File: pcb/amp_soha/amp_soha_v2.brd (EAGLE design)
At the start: 83.9 x 48.9 mm, 59 parts, among them IC1 NE5535U, IC2 7812, IC3 7912, Q1 J113, Q2 J113, Q3 J113, Q4 J113

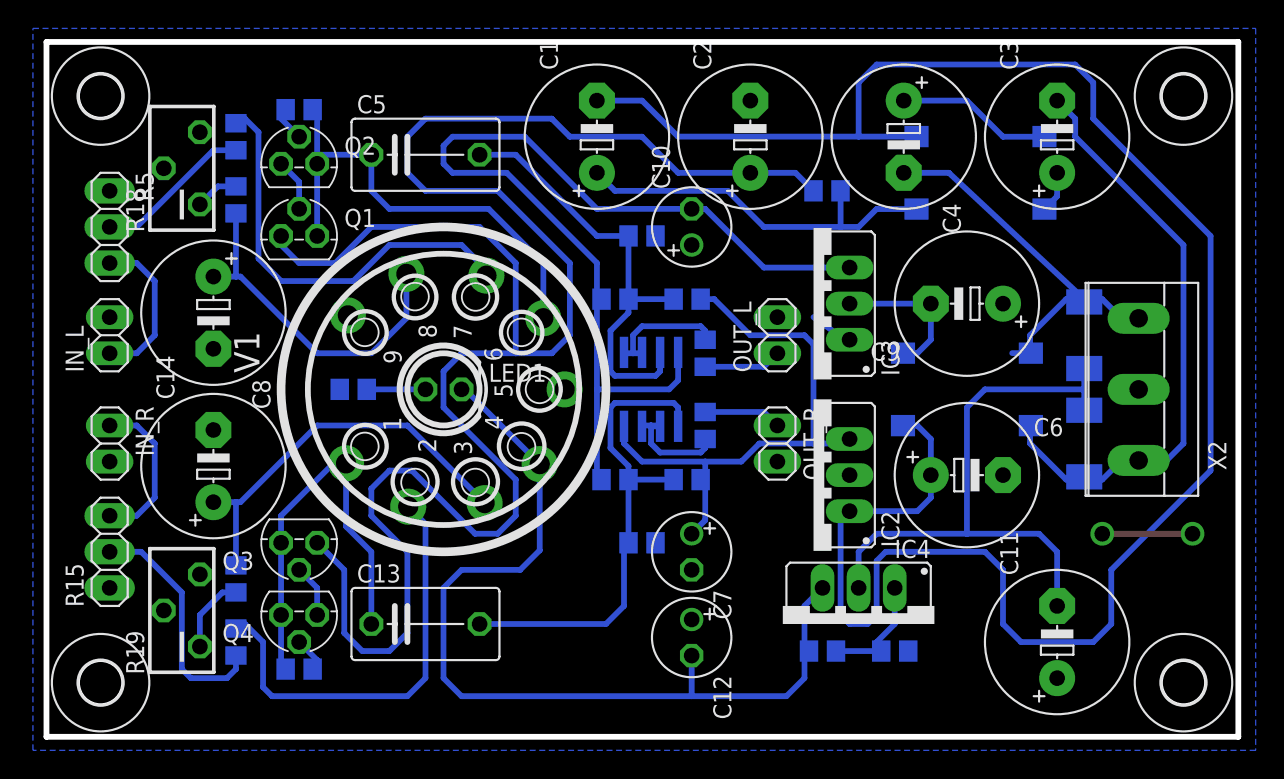
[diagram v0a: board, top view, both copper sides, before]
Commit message: 
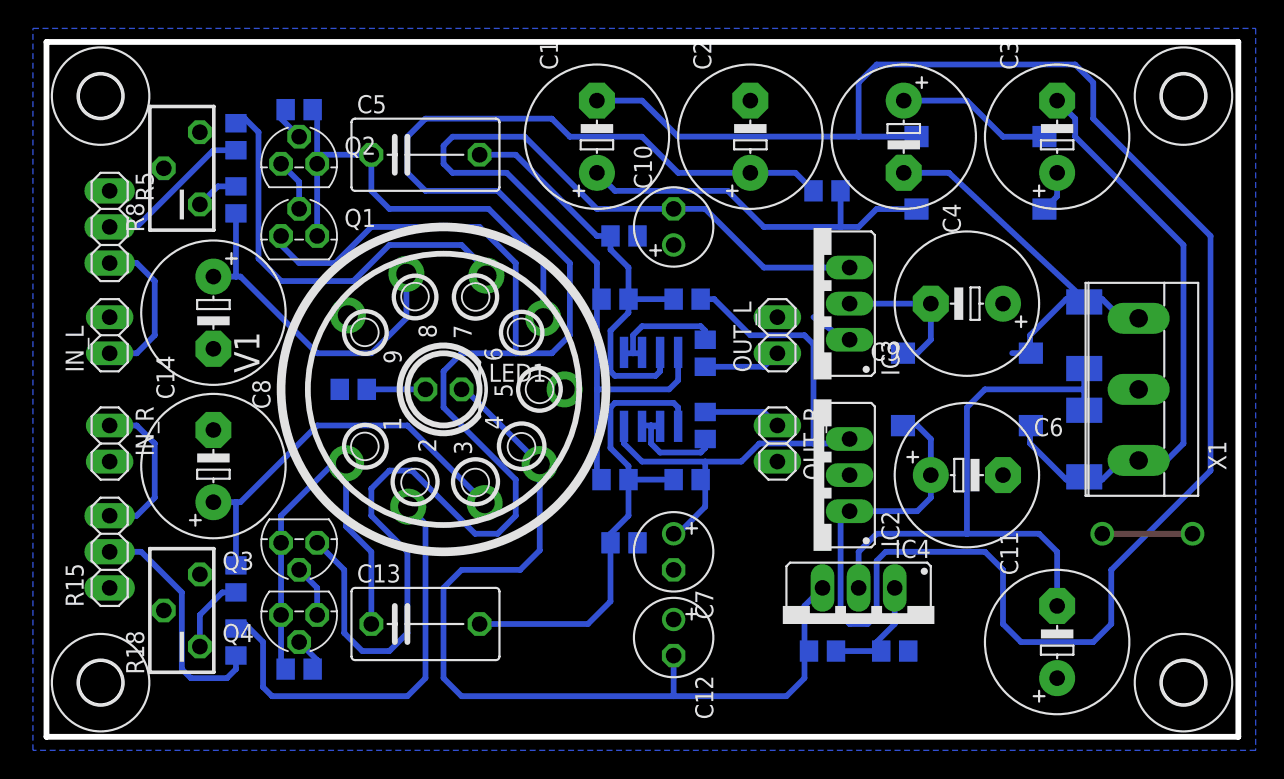
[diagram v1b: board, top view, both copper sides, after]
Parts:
- removed R19: (no value), amp_soha:RTRIM3296Y
- added R8: 2k, amp_soha:RTRIM3296Y
- R10: value (none) -> 1k
- R12, R2: value 360 -> 1k5
- R18: value (none) -> 2k
- moved R18 31.1 mm to (12.1, 9.84)
- moved C10 1.27 mm to (46.7, 36.8)
- moved C12 1.27 mm to (46.7, 7.94)
- moved C7 1.27 mm to (46.7, 14.0)
- moved R14 1.27 mm to (43.2, 14.6)
- moved R4 1.27 mm to (43.2, 36.2)
- renumbered X2 to X1
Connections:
- net AGND: now also R8.2, R8.3; no longer R19.2, R19.3
- net N$17: now also R8.1; no longer R18.1
- net N$18: now also R18.1; no longer R19.1
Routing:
- net N$34: track 35.9 -> 34.4 mm
- net N$22: track 33.1 -> 32.0 mm
- net +12V: track 41.5 -> 42.2 mm

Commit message: 
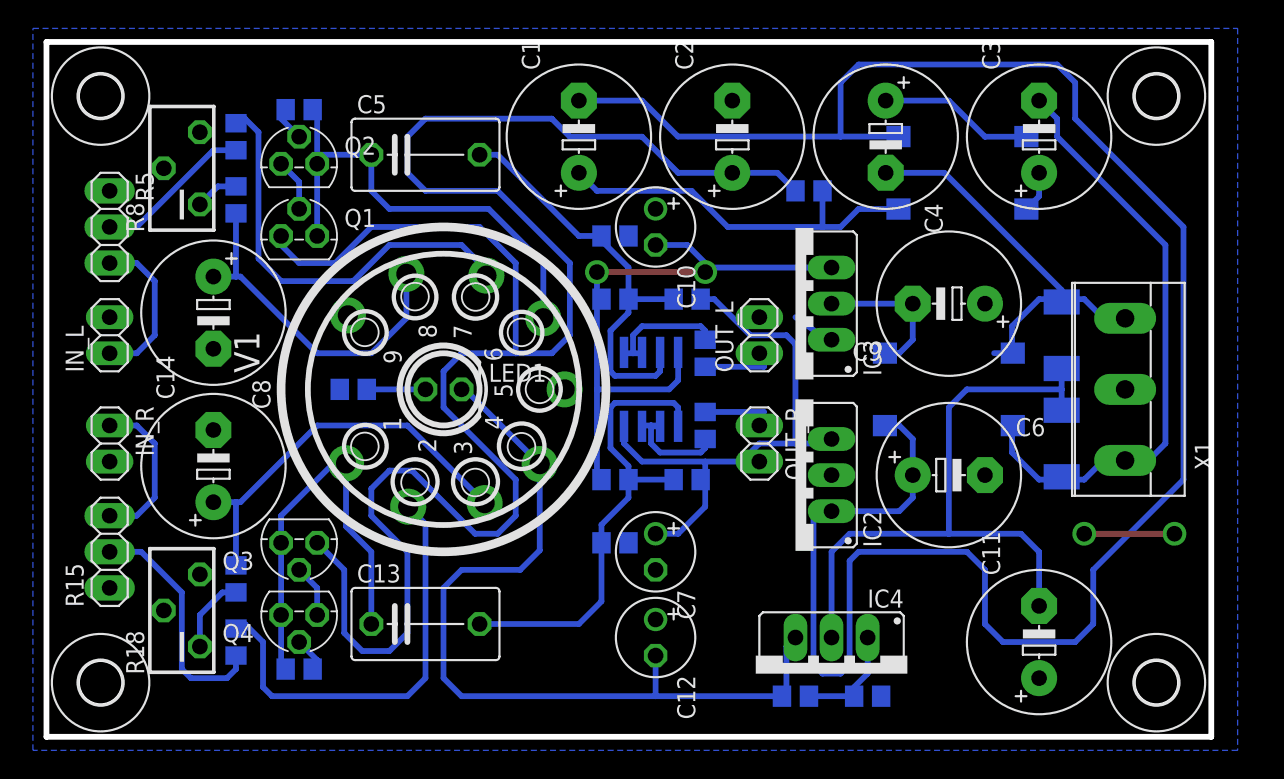
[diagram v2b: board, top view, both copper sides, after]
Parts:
- moved IC4 3.98 mm to (57.8, 5.40)
- moved R9 3.70 mm to (55.2, 3.81)
- moved R11 3.70 mm to (60.3, 3.81)
- moved U$3 1.91 mm to (80.6, 4.76)
- moved U$4 1.91 mm to (80.6, 46.0)
- moved D3 1.59 mm to (74.0, 21.6)
- moved D4 1.59 mm to (74.0, 29.2)
- moved C2 1.27 mm to (50.8, 43.2)
- moved C4 1.27 mm to (61.6, 43.2)
- moved IC2 1.27 mm to (55.2, 19.4)
- moved IC3 1.27 mm to (55.2, 31.4)
- moved OUT_L 1.27 mm to (52.7, 29.2)
- moved OUT_R 1.27 mm to (52.7, 21.6)
- moved R1 1.27 mm to (56.2, 39.4)
- moved B1 1.27 mm to (67.0, 40.6)
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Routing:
- net -12V: track 72.0 -> 45.1 mm, vias 0 -> 2
- net N$6: track 138.9 -> 146.6 mm
- net -12.6V: track 64.4 -> 59.7 mm
- net N$3: track 42.0 -> 45.8 mm
- net N$2: track 28.4 -> 31.0 mm
- net N$1: track 42.3 -> 43.6 mm
- net +12V: track 42.2 -> 41.0 mm
- net +24V: track 138.1 -> 136.9 mm
- net N$4: track 8.28 -> 7.70 mm
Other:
- board size 83.9 x 48.9 mm -> 82 x 48.9 mm

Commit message: 
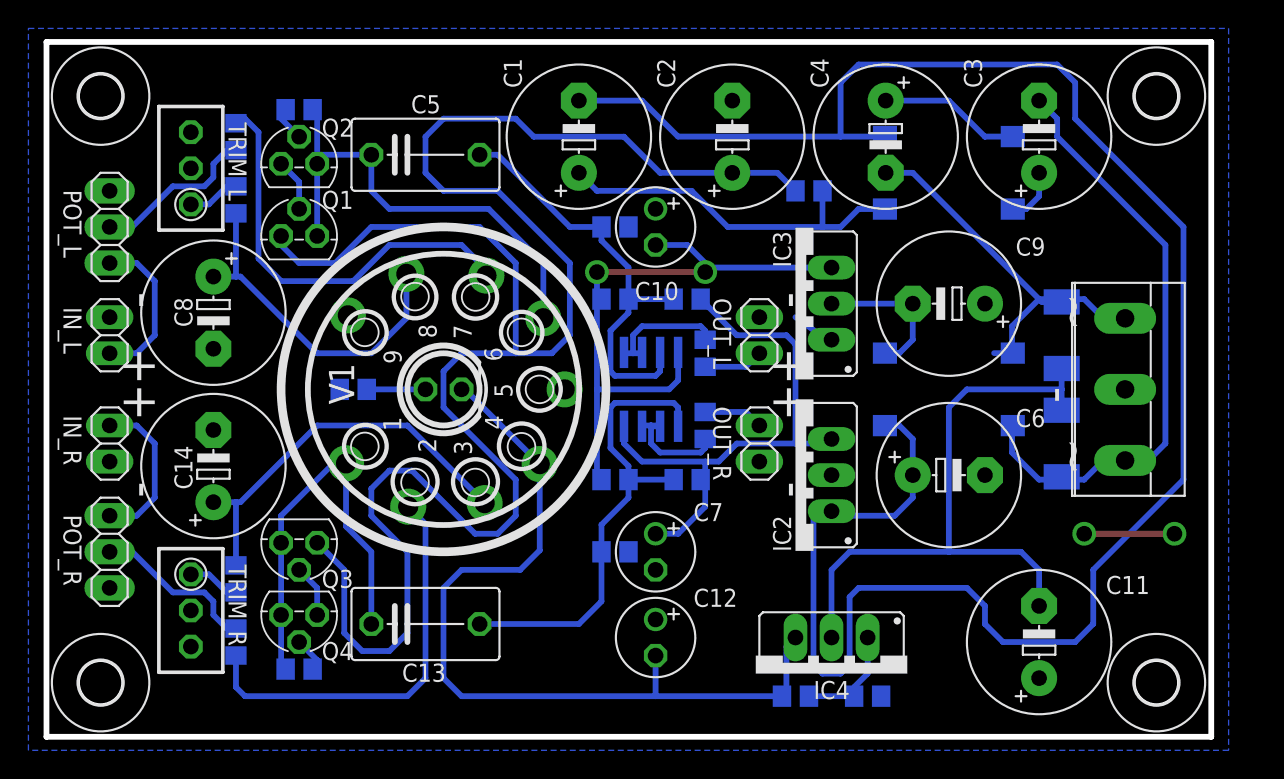
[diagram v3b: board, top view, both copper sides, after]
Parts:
- removed R18, R8: 2k, amp_soha:RTRIM3296Y
- added TRIM_L, TRIM_R: 2k, amp_soha:RTRIM3296W
- moved B1 0.95 mm to (66.0, 40.6)
- moved R14 0.63 mm to (42.5, 14.0)
- moved R4 0.63 mm to (42.5, 36.8)
- turned R16 to 90 degrees
- renumbered R15 to POT_R, R5 to POT_L
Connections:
- net AGND: now also TRIM_L.2, TRIM_L.3, TRIM_R.2, TRIM_R.3; no longer R18.2, R18.3, R8.2, R8.3
- net N$17: now also TRIM_L.1; no longer R8.1
- net N$18: now also TRIM_R.1; no longer R18.1
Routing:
- net N$6: track 146.6 -> 140.7 mm
- net N$27: track 17.0 -> 12.0 mm
- net +24V: track 136.9 -> 134.3 mm
- net N$10: track 30.7 -> 28.9 mm
- net N$18: track 5.42 -> 3.70 mm
- net N$3: track 45.8 -> 44.5 mm
- net N$9: track 11.0 -> 10.0 mm
- net N$8: track 2.92 -> 3.87 mm
- net N$11: track 27.1 -> 26.2 mm
- net N$25: track 5.13 -> 4.20 mm
- net N$36: track 5.13 -> 4.20 mm
- net +12V: track 41.0 -> 40.3 mm
- net N$17: track 3.07 -> 3.70 mm
- net N$13: track 11.1 -> 11.7 mm
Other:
- board text added: "+"
- board text added: "-"
- board text added: "~"
